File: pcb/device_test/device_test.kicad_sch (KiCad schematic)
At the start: 4 parts, among them J101 Screw_Terminal_01x02

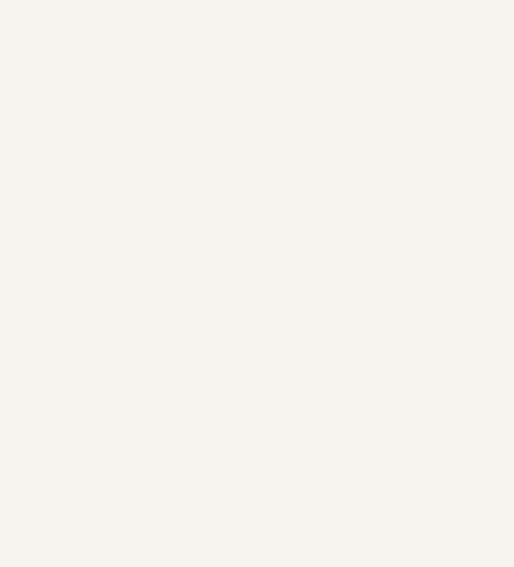
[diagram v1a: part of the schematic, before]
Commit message: change mounting hole
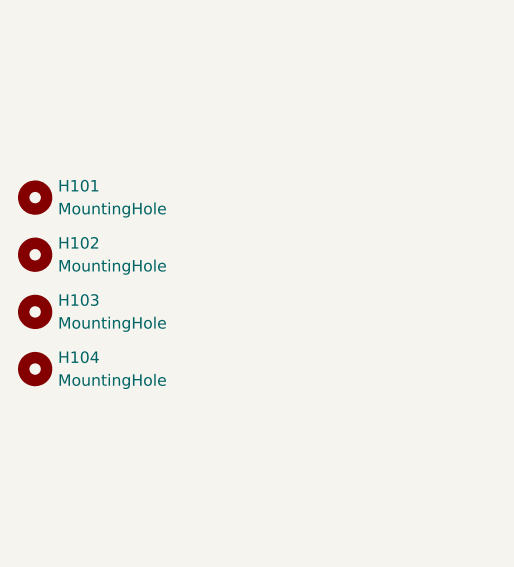
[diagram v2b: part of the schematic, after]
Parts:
- added H101, H102, H103, H104: MountingHole, MountingHole:MountingHole_3.2mm_M3, symbol Mechanical:MountingHole

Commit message: update ALL parts
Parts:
- C101: footprint Capacitor_Tantalum_SMD:CP_EIA-7343-43_Kemet-X_Pad2.25x2.55mm_HandSolder -> Capacitor_Tantalum_SMD:CP_EIA-7343-43_Kemet-X; LCSC C7230 -> C132558
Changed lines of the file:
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@@
 			)
 		)
-		(property "Footprint" "Capacitor_Tantalum_SMD:CP_EIA-7343-43_Kemet-X_Pad2.25x2.55mm_HandSolder"
+		(property "Footprint" "Capacitor_Tantalum_SMD:CP_EIA-7343-43_Kemet-X"
 			(at 131.7752 91.44 0)
 			(effects
@@
 			)
 		)
-		(property "LCSC" "C7230"
+		(property "LCSC" "C132558"
 			(at 130.81 87.63 0)
 			(effects
@@
 				)
 				(hide yes)
+			)
+		)
+		(property "MOUSER" ""
+			(at 130.81 87.63 0)
+			(effects
+				(font
+					(size 1.27 1.27)
+				)
 			)
 		)
@@
 			)
 		)
+		(property "MOUSER" ""
+			(at 38.1 139.7 0)
+			(effects
+				(font
+					(size 1.27 1.27)
+				)
+			)
+		)
 		(instances
 			(project ""
@@
 			)
 		)
+		(property "MOUSER" ""
+			(at 38.1 146.05 0)
+			(effects
+				(font
+					(size 1.27 1.27)
+				)
+			)
+		)
 		(instances
 			(project "device_test"
@@
 			)
 		)
+		(property "MOUSER" ""
+			(at 38.1 158.75 0)
+			(effects
+				(font
+					(size 1.27 1.27)
+				)
+			)
+		)
 		(instances
 			(project "device_test"
@@
 			)
 		)
+		(property "MOUSER" ""
+			(at 38.1 152.4 0)
+			(effects
+				(font
+					(size 1.27 1.27)
+				)
+			)
+		)
 		(instances
 			(project "device_test"
@@
 			)
 		)
+		(property "MOUSER" ""
+			(at 93.98 99.06 0)
+			(effects
+				(font
+					(size 1.27 1.27)
+				)
+			)
+		)
 		(pin "1"
 		)
@@
 			)
 		)
+		(property "MOUSER" ""
+			(at 69.85 86.36 0)
+			(effects
+				(font
+					(size 1.27 1.27)
+				)
+			)
+		)
 		(pin "2"
 		)
@@
 			)
 		)
+		(property "MOUSER" ""
+			(at 69.85 96.52 0)
+			(effects
+				(font
+					(size 1.27 1.27)
+				)
+			)
+		)
